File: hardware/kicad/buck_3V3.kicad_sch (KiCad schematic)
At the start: 8 parts, among them J1 Screw_Terminal_01x02, J2 Screw_Terminal_01x02, U1 PTSM82903SISB2R

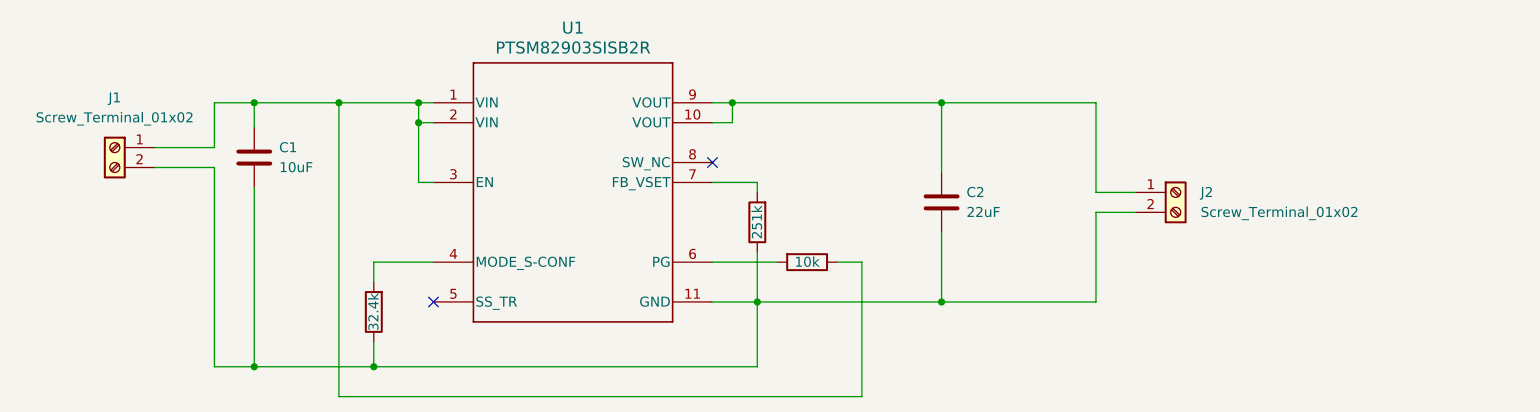
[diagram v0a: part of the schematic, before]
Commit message: docs: edited end-semester-report
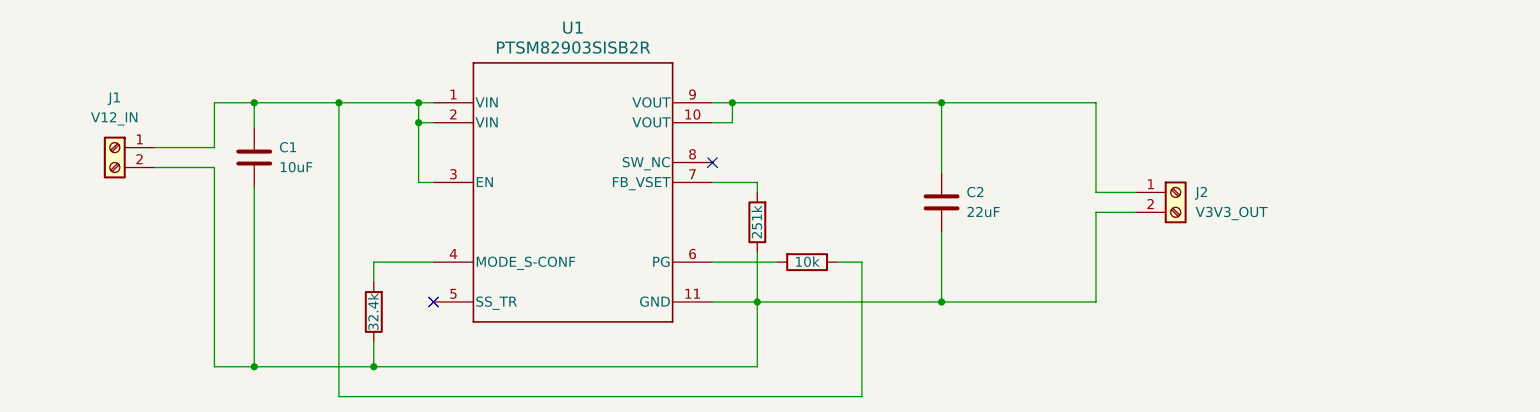
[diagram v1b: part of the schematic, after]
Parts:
- J1: value Screw_Terminal_01x02 -> V12_IN
- J2: value Screw_Terminal_01x02 -> V3V3_OUT
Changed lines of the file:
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@@
       (effects (font (size 1.27 1.27)))
     )
-    (property "Value" "Screw_Terminal_01x02" (at 102.235 83.82 0)
+    (property "Value" "V12_IN" (at 102.235 83.82 0)
       (effects (font (size 1.27 1.27)))
     )
@@
   (symbol (lib_id "Connector:Screw_Terminal_01x02") (at 237.49 93.345 0) (unit 1)
     (in_bom yes) (on_board yes) (dnp no) (fields_autoplaced)
-    (property "Reference" "J2" (at 240.665 93.345 0)
+    (property "Reference" "J2" (at 240.03 93.345 0)
       (effects (font (size 1.27 1.27)) (justify left))
     )
-    (property "Value" "Screw_Terminal_01x02" (at 240.665 95.885 0)
+    (property "Value" "V3V3_OUT" (at 240.03 95.885 0)
       (effects (font (size 1.27 1.27)) (justify left))
     )

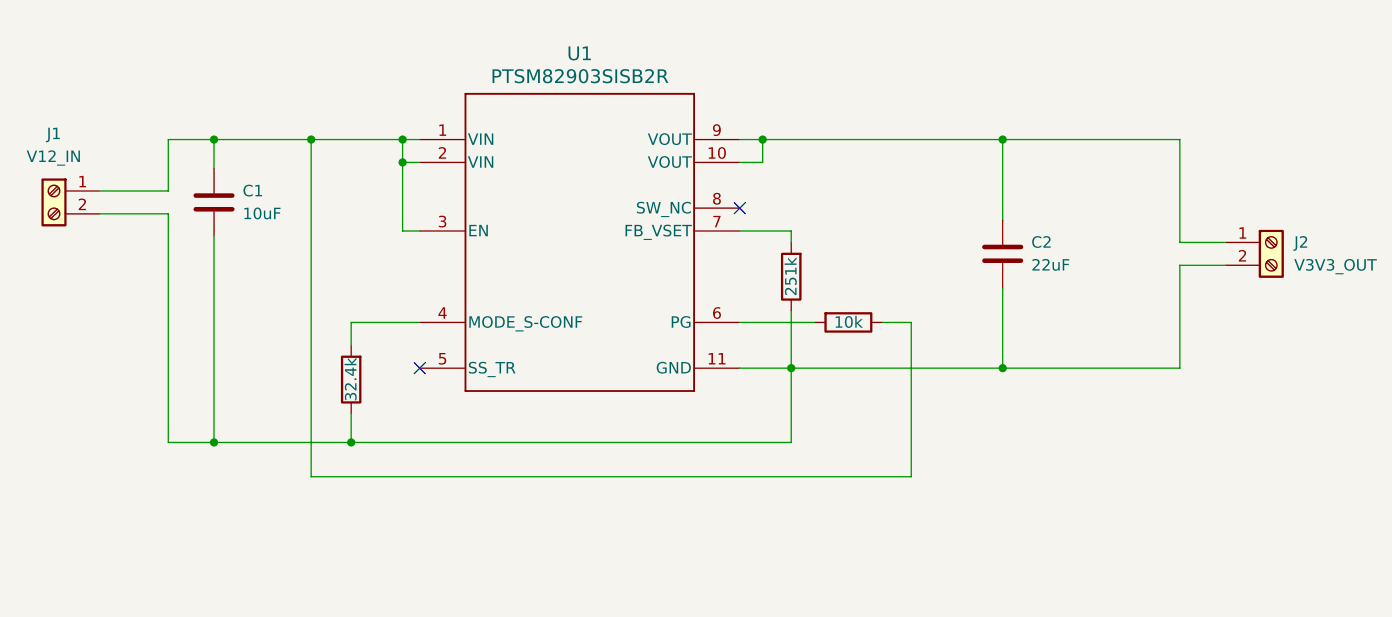
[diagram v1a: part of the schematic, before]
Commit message: feat: added pcb to buck3V3
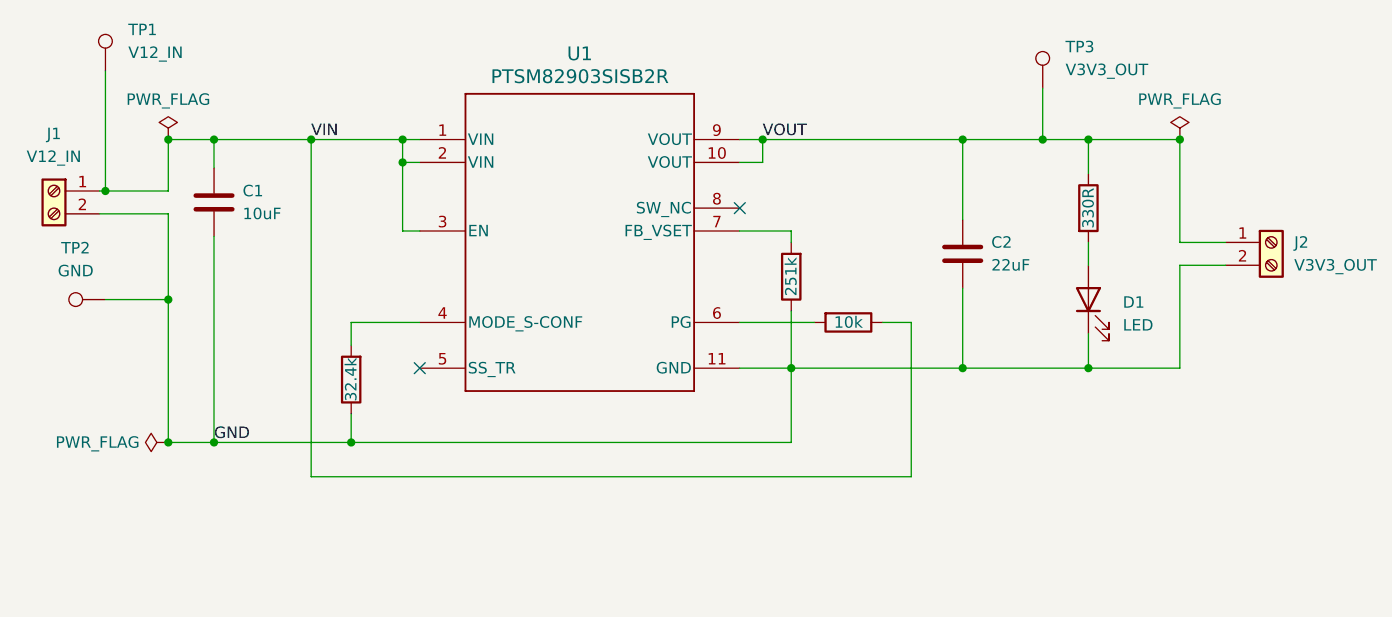
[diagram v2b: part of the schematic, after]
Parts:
- added D1: LED, LED_THT:LED_D3.0mm, symbol Device:LED
- added R4: 330R, Resistor_THT:R_Axial_DIN0207_L6.3mm_D2.5mm_P10.16mm_Horizontal, symbol Device:R
- added TP1: V12_IN, TestPoint:TestPoint_Pad_D2.5mm, symbol Connector:TestPoint
- added TP2: GND, TestPoint:TestPoint_Pad_D2.5mm, symbol Connector:TestPoint
- added TP3: V3V3_OUT, TestPoint:TestPoint_Pad_D2.5mm, symbol Connector:TestPoint
- C1, C2: footprint (none) -> Capacitor_THT:C_Rect_L7.0mm_W3.5mm_P5.00mm
- J1, J2: footprint (none) -> Terminals:CUI_TB002-500-02BE
- R1, R2, R3: footprint (none) -> Resistor_THT:R_Axial_DIN0207_L6.3mm_D2.5mm_P10.16mm_Horizontal
- U1: footprint SIS0011A-MFG -> buck_3V3:SIS0011A-MFG
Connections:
- net VIN: now reaches C1.1, J1.1 (Pin_1), R3.1, U1.1 (VIN), U1.2 (VIN), U1.3 (EN)
- net VIN: now also TP1.1
- net VOUT: now reaches C2.1, J2.1 (Pin_1), U1.10 (VOUT), U1.9 (VOUT)
- net VOUT: now also R4.1, TP3.1
- net GND: now reaches C1.2, C2.2, J1.2 (Pin_2), J2.2 (Pin_2), R1.1, R2.1, U1.11 (GND)
- net GND: now also D1.1 (K), TP2.1
- new net: D1.2 (A), R4.2
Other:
- moved on the sheet: C2

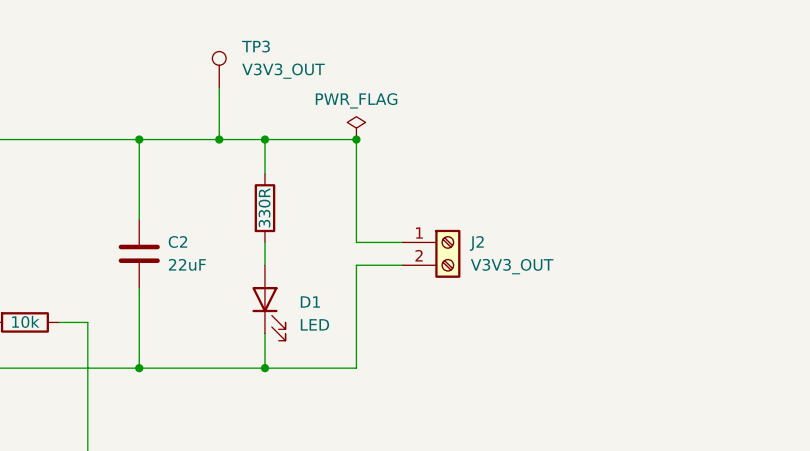
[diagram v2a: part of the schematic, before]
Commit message: feat: added pcb for buck 5V1
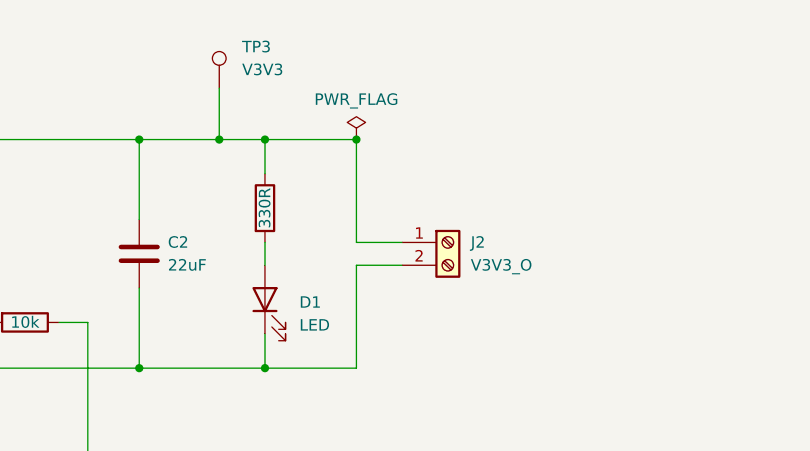
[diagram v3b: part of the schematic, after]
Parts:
- J2: value V3V3_OUT -> V3V3_O
- TP3: value V3V3_OUT -> V3V3
- U1: footprint buck_3V3:SIS0011A-MFG -> SIS0011A-MFG
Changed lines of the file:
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@@
       (effects (font (size 1.524 1.524)))
     )
-    (property "Footprint" "buck_3V3:SIS0011A-MFG" (at 142.875 81.915 0)
+    (property "Footprint" "SIS0011A-MFG" (at 142.875 81.915 0)
       (effects (font (size 1.27 1.27) italic) hide)
     )
@@
       (effects (font (size 1.27 1.27)) (justify left))
     )
-    (property "Value" "V3V3_OUT" (at 240.03 95.885 0)
+    (property "Value" "V3V3_O" (at 240.03 95.885 0)
       (effects (font (size 1.27 1.27)) (justify left))
     )
@@
       (effects (font (size 1.27 1.27)) (justify left))
     )
-    (property "Value" "V3V3_OUT" (at 214.63 74.168 0)
-      (effects (font (size 1.27 1.27)) (justify left))
-    )
+    (property "Value" "V3V3" (at 214.63 74.168 0)
+      (effects (font (size 1.27 1.27)) (justify left))
+    )
